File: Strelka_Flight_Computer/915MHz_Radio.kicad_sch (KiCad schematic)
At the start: 4 parts, among them U4 RFM95W-915S2

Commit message: Started design for V2
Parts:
- AE1: footprint Connector_Coaxial:SMA_Amphenol_132134_Vertical -> Footprints:STA-10201; LCSC# C496550 -> C2913580
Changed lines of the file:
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@@
       (effects (font (size 1.27 1.27)) (justify left))
     )
-    (property "Footprint" "Connector_Coaxial:SMA_Amphenol_132134_Vertical" (at 166.37 80.645 0)
+    (property "Footprint" "Footprints:STA-10201" (at 166.37 80.645 0)
       (effects (font (size 1.27 1.27)) hide)
     )
-    (property "Datasheet" "~" (at 166.37 80.645 0)
+    (property "Datasheet" "https://datasheet.lcsc.com/lcsc/2111030930_STA-STA-10201_C2913580.pdf" (at 166.37 80.645 0)
       (effects (font (size 1.27 1.27)) hide)
     )
-    (property "LCSC#" "C496550" (at 166.37 83.185 0)
+    (property "LCSC#" "C2913580" (at 166.37 83.185 0)
       (effects (font (size 1.27 1.27)) hide)
     )

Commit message: Continued routing
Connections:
- net LoRa_Sig: now reaches AE1.1 (A), U4.9 (ANT)
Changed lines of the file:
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@@
     (stroke (width 0) (type solid))
+  )
+  (label "LoRa_Sig" (at 160.401 88.265 0) (fields_autoplaced)
+    (effects (font (size 1.27 1.27)) (justify left bottom))
   )
   (hierarchical_label "SPI_MISO" (shape input) (at 132.08 93.345 180) (fields_autoplaced)

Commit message: Routing complete
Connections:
- net +3V3 renamed +3.3V
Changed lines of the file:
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@@
+    )
+  )
+  (symbol (lib_name "+3.3V_1") (lib_id "power:+3.3V") (at 97.79 86.995 0) (unit 1)
+    (in_bom yes) (on_board yes) (dnp no) (fields_autoplaced)
+    (property "Reference" "#PWR019" (at 97.79 90.805 0)
+      (effects (font (size 1.27 1.27)) hide)
+    )
+    (property "Value" "+3.3V" (at 97.79 83.185 0)
+      (effects (font (size 1.27 1.27)))
+    )
+    (property "Footprint" "" (at 97.79 86.995 0)
+      (effects (font (size 1.27 1.27)) hide)
+    )
+    (property "Datasheet" "" (at 97.79 86.995 0)
+      (effects (font (size 1.27 1.27)) hide)
+    )
+    (pin "1")
+    (instances
+      (project "Strelka_Flight_Computer"
+        (path "/e63e39d7-6ac0-4ffd-8aa3-1841a4541b55/72745e37-6398-4523-a0b8-fcae44c9df22"
+          (reference "#PWR019") (unit 1)
+        )
+      )
     )
   )
@@
     )
   )
-  (symbol (lib_id "power:+3.3V") (at 147.32 83.185 0) (unit 1)
+  (symbol (lib_name "+3.3V_1") (lib_id "power:+3.3V") (at 147.32 83.185 0) (unit 1)
     (in_bom yes) (on_board yes) (dnp no) (fields_autoplaced)
-    (property "Reference" "#PWR0123" (at 147.32 86.995 0)
+    (property "Reference" "#PWR020" (at 147.32 86.995 0)
       (effects (font (size 1.27 1.27)) hide)
     )
-    (property "Value" "+3.3V" (at 147.32 79.6092 0)
+    (property "Value" "+3.3V" (at 147.32 79.375 0)
       (effects (font (size 1.27 1.27)))
     )
@@
       (project "Strelka_Flight_Computer"
         (path "/e63e39d7-6ac0-4ffd-8aa3-1841a4541b55/72745e37-6398-4523-a0b8-fcae44c9df22"
-          (reference "#PWR0123") (unit 1)
+          (reference "#PWR020") (unit 1)
         )
       )
-    )
-  )
-  (symbol (lib_id "power:+3.3V") (at 97.79 86.995 0) (unit 1)
-    (in_bom yes) (on_board yes) (dnp no) (fields_autoplaced)
-    (property "Reference" "#PWR0122" (at 97.79 90.805 0)
-      (effects (font (size 1.27 1.27)) hide)
-    )
-    (property "Value" "+3.3V" (at 97.79 83.4192 0)
-      (effects (font (size 1.27 1.27)))
-    )
-    (property "Footprint" "" (at 97.79 86.995 0)
-      (effects (font (size 1.27 1.27)) hide)
-    )
-    (property "Datasheet" "" (at 97.79 86.995 0)
-      (effects (font (size 1.27 1.27)) hide)
-    )
-    (pin "1")
-    (instances
-      (project "Strelka_Flight_Computer"
-        (path "/e63e39d7-6ac0-4ffd-8aa3-1841a4541b55/72745e37-6398-4523-a0b8-fcae44c9df22"
-          (reference "#PWR0122") (unit 1)
-        )
-      )

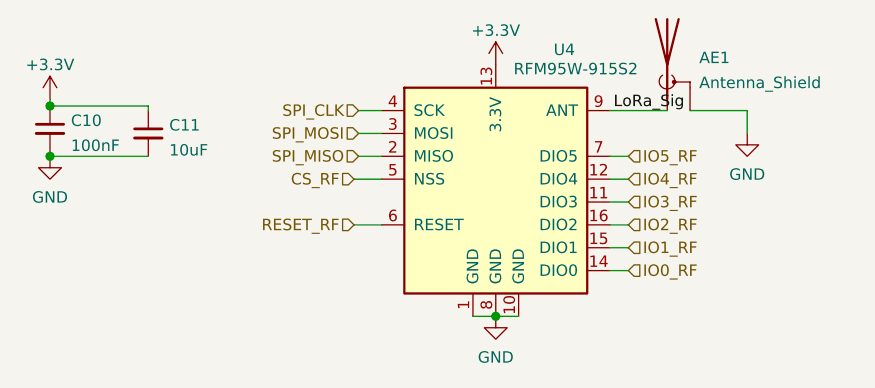
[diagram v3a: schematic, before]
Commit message: Created BOM
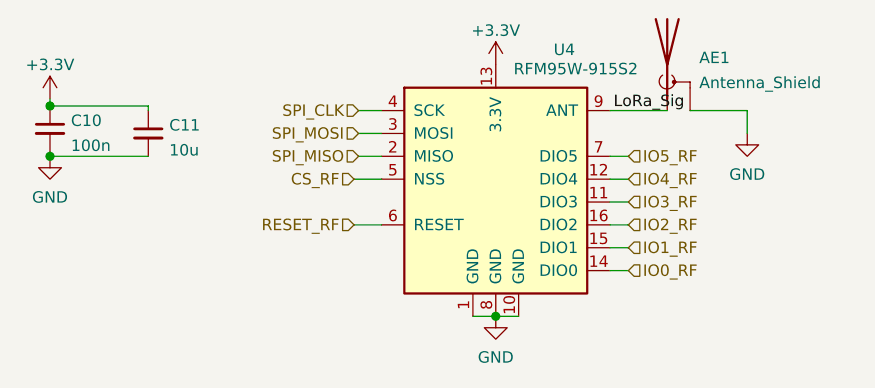
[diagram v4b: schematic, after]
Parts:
- AE1: LCSC (none) -> C2913580; LCSC# C2913580 -> (none)
- C10: value 100nF -> 100n
- C11: value 10uF -> 10u
- U4: LCSC (none) -> C2844473; LCSC# C2844473 -> (none)
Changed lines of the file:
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@@
       (effects (font (size 1.27 1.27)) hide)
     )
-    (property "LCSC#" "C2844473" (at 147.32 95.885 0)
+    (property "LCSC" "C2844473" (at 147.32 95.885 0)
       (effects (font (size 1.27 1.27)) hide)
     )
@@
       (effects (font (size 1.27 1.27)) (justify left))
     )
-    (property "Value" "10uF" (at 111.0362 92.6716 0)
+    (property "Value" "10u" (at 111.0362 92.6716 0)
       (effects (font (size 1.27 1.27)) (justify left))
     )
@@
       (effects (font (size 1.27 1.27)) hide)
     )
-    (property "LCSC#" "C2913580" (at 166.37 83.185 0)
+    (property "LCSC" "C2913580" (at 166.37 83.185 0)
       (effects (font (size 1.27 1.27)) hide)
     )
@@
       (effects (font (size 1.27 1.27)) (justify left))
     )
-    (property "Value" "100nF" (at 100.1142 92.1636 0)
+    (property "Value" "100n" (at 100.1142 92.1636 0)
       (effects (font (size 1.27 1.27)) (justify left))
     )

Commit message: Added LCSC mpn to all relevent parts
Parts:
- C10: footprint Capacitor_SMD:C_0603_1608Metric_Pad1.08x0.95mm_HandSolder -> Capacitor_SMD:C_0402_1005Metric; LCSC (none) -> C1525
- C11: LCSC (none) -> C19702
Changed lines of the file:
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@@
+      (effects (font (size 1.27 1.27)) hide)
+    )
+    (property "LCSC" " C19702" (at 108.712 90.805 0)
       (effects (font (size 1.27 1.27)) hide)
     )
@@
       (effects (font (size 1.27 1.27)) (justify left))
     )
-    (property "Footprint" "Capacitor_SMD:C_0603_1608Metric_Pad1.08x0.95mm_HandSolder" (at 97.79 90.297 0)
+    (property "Footprint" "Capacitor_SMD:C_0402_1005Metric" (at 97.79 90.297 0)
       (effects (font (size 1.27 1.27)) hide)
     )
@@
       (effects (font (size 1.27 1.27)) hide)
     )
+    (property "LCSC" " C1525" (at 97.79 90.297 0)
+      (effects (font (size 1.27 1.27)) hide)
+    )
